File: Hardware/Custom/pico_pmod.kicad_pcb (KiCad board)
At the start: 2 copper layers, 50 x 37 mm, 35 parts, among them J1 Conn_02x06_Odd_Even, J2 Conn_02x06_Odd_Even, J3 Conn_02x06_Odd_Even, J4 USB_C_Receptacle_USB2.0, J5 Conn_01x04, SW1 SW_Push, SW2 SW_Push, U1 RP2040, U2 W25Q128JVS, U3 NCP1117-3.3_SOT223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

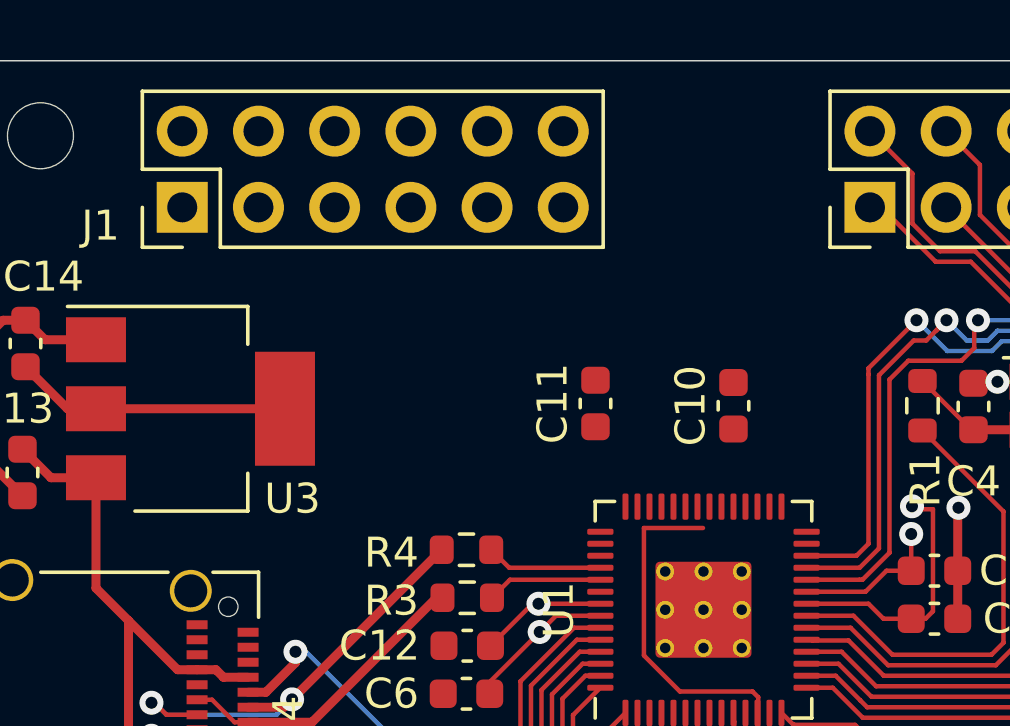
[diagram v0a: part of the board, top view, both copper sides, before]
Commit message: Add connections to PMOD1A connector
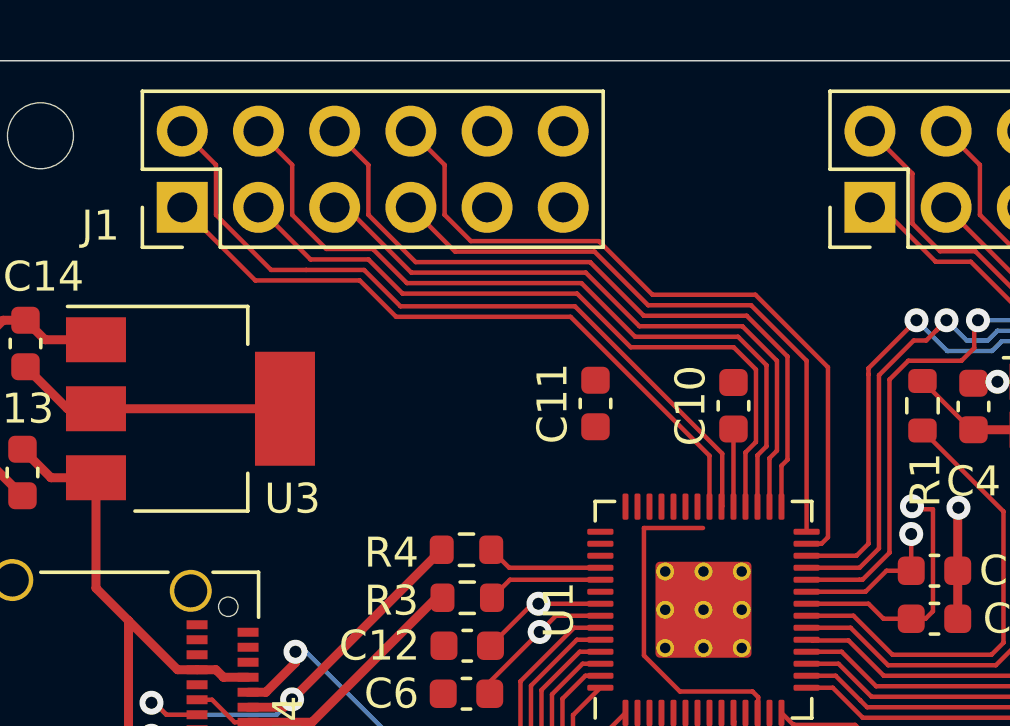
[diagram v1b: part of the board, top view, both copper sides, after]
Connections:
- J1 pad 1: Net-(J1-Pad1) -> GPIO_23
- J1 pad 2: Net-(J1-Pad2) -> GPIO_22
- J1 pad 3: Net-(J1-Pad3) -> GPIO_21
- J1 pad 4: Net-(J1-Pad4) -> GPIO_20
- J1 pad 5: Net-(J1-Pad5) -> GPIO_19
- J1 pad 6: Net-(J1-Pad6) -> GPIO_18
- J1 pad 7: Net-(J1-Pad7) -> GPIO_17
- J1 pad 8: Net-(J1-Pad8) -> GPIO_16
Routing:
- net GPIO_20: track 0.00 -> 26.0 mm
- net GPIO_22: track 0.00 -> 25.2 mm
- net GPIO_16: track 0.00 -> 24.6 mm
- net GPIO_18: track 0.00 -> 24.3 mm
- net GPIO_21: track 0.00 -> 23.5 mm
- net GPIO_23: track 0.00 -> 22.7 mm
- net GPIO_19: track 0.00 -> 21.8 mm
- net GPIO_17: track 0.00 -> 21.0 mm
- net +3V3: track 47.2 -> 49.8 mm

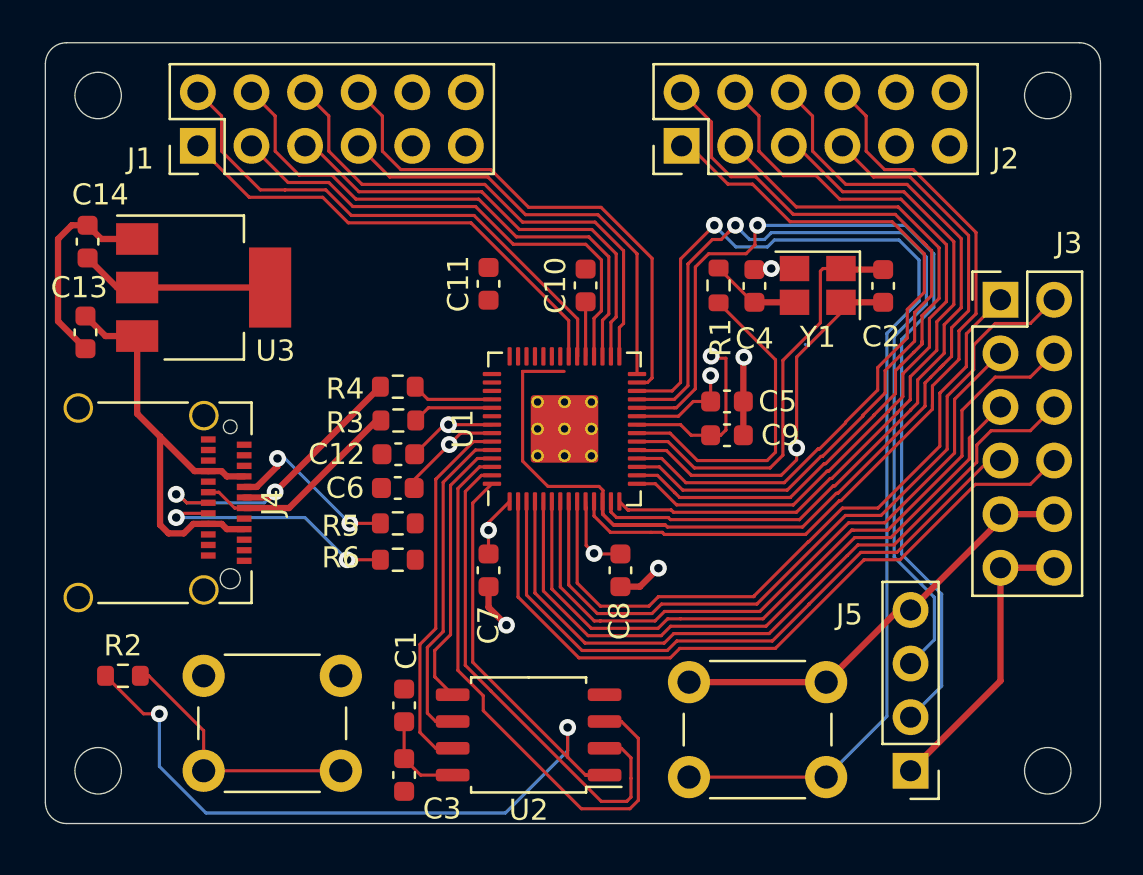
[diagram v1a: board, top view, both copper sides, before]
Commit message: update with ground plane and LED's
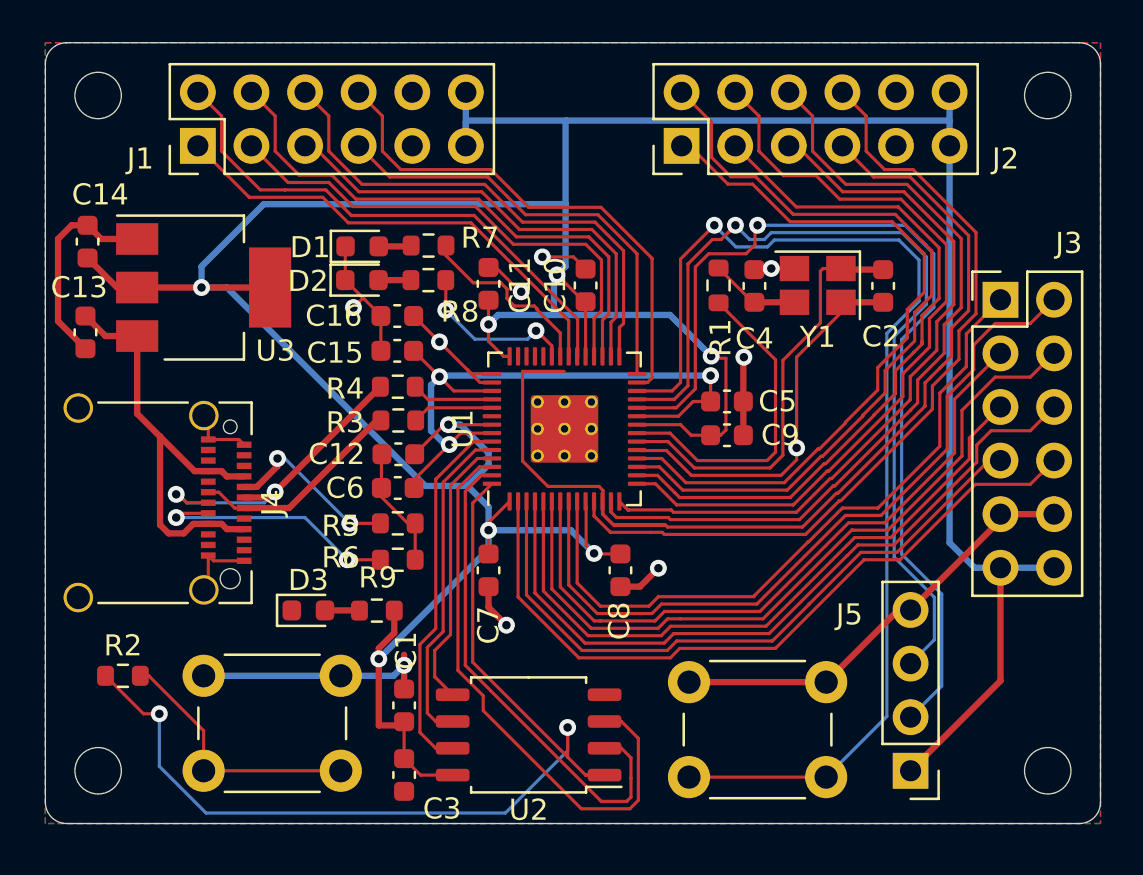
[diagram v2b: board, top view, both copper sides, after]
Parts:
- added C15: 1u, Capacitor_SMD:C_0603_1608Metric, F.Cu at (139.7, 71.6)
- added C16: 1u, Capacitor_SMD:C_0603_1608Metric, F.Cu at (139.7, 70.0)
- added D1: LED, LED_SMD:LED_0603_1608Metric, F.Cu at (138.0, 66.7)
- added D2: LED, LED_SMD:LED_0603_1608Metric, F.Cu at (138.0, 68.2)
- added D3: LED, LED_SMD:LED_0603_1608Metric, F.Cu at (135.5, 83.9)
- added R7: R, Resistor_SMD:R_0603_1608Metric, F.Cu at (141.2, 66.6)
- added R8: R, Resistor_SMD:R_0603_1608Metric, F.Cu at (141.2, 68.2)
- added R9: R, Resistor_SMD:R_0603_1608Metric, F.Cu at (138.7, 83.9)
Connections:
- U1 pad 37: Net-(U1-Pad37) -> GPIO_25
- U1 pad 43: Net-(U1-Pad43) -> +3V3
- U1 pad 44: Net-(U1-Pad44) -> +3V3
- U1 pad 45: Net-(U1-Pad45) -> +1V1
- U1 pad 48: Net-(U1-Pad48) -> +3V3
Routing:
- net +3V3: track 49.8 -> 196.7 mm, vias 4 -> 9
- net GND: track 59.5 -> 93.4 mm, vias 5 -> 9
- net +1V1: track 10.0 -> 31.3 mm, vias 2 -> 3
- net GPIO_24: track 0.00 -> 8.82 mm
- net GPIO_25: track 0.00 -> 7.98 mm, vias 0 -> 2
- net Net-(D3-Pad2): track 0.00 -> 1.64 mm
- net Net-(D1-Pad2): track 0.00 -> 1.55 mm
- net Net-(D2-Pad2): track 0.00 -> 1.54 mm
- added copper zone on B.Cu, net GND
- added copper zone on F.Cu, net GND

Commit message: Add the logo and text onto back of the PCB
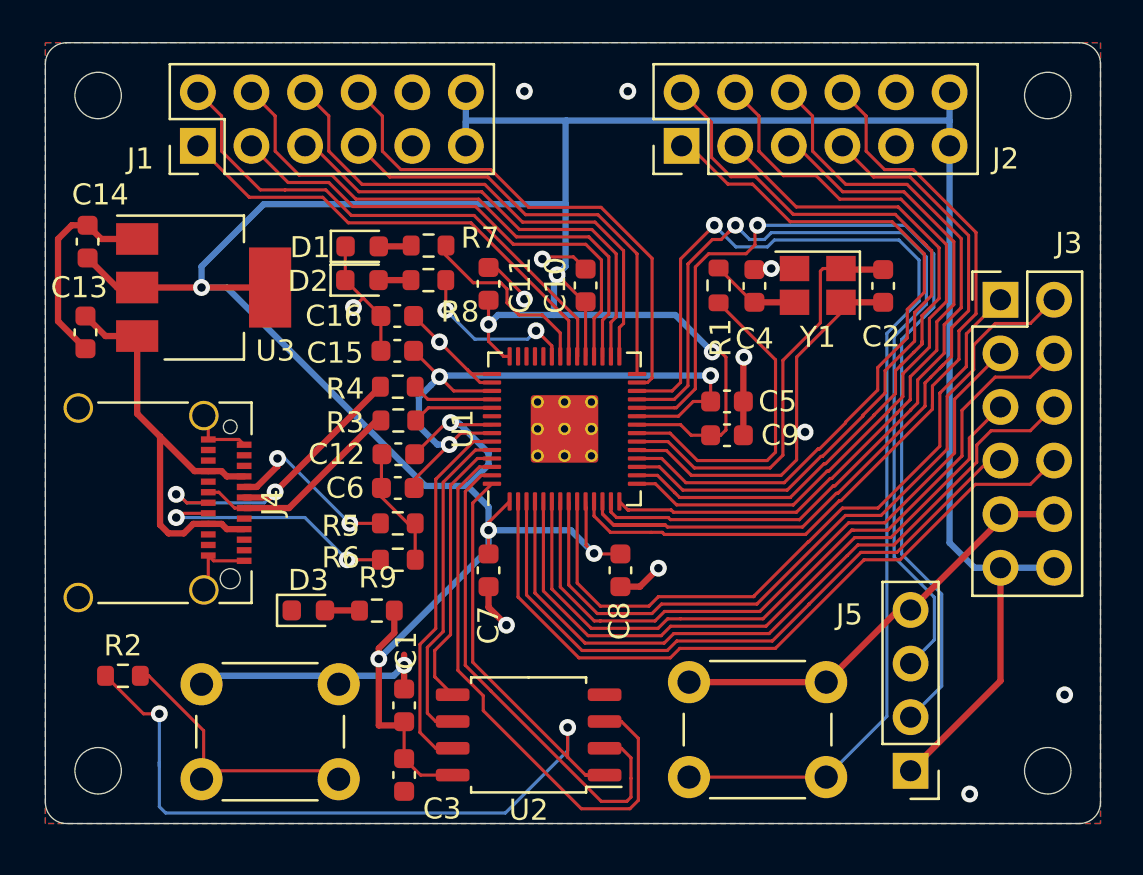
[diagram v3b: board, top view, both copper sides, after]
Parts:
- added G***: LOGO, jjh:Untitled, B.Cu at (155.0, 76.2)
- moved SW1 0.41 mm to (130.4, 87.4)
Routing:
- net GPIO_9: track 50.3 -> 38.6 mm
- net QSPI_SS: track 47.9 -> 49.2 mm
- net +1V1: track 31.3 -> 32.2 mm
- net GND: track 93.4 -> 94.3 mm, vias 9 -> 13
- net +3V3: track 196.7 -> 197.3 mm
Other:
- board text added: "RP2040 PMod Board @jamesjhorton jjhorton.co.uk"

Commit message: Add lables to the Debug Port
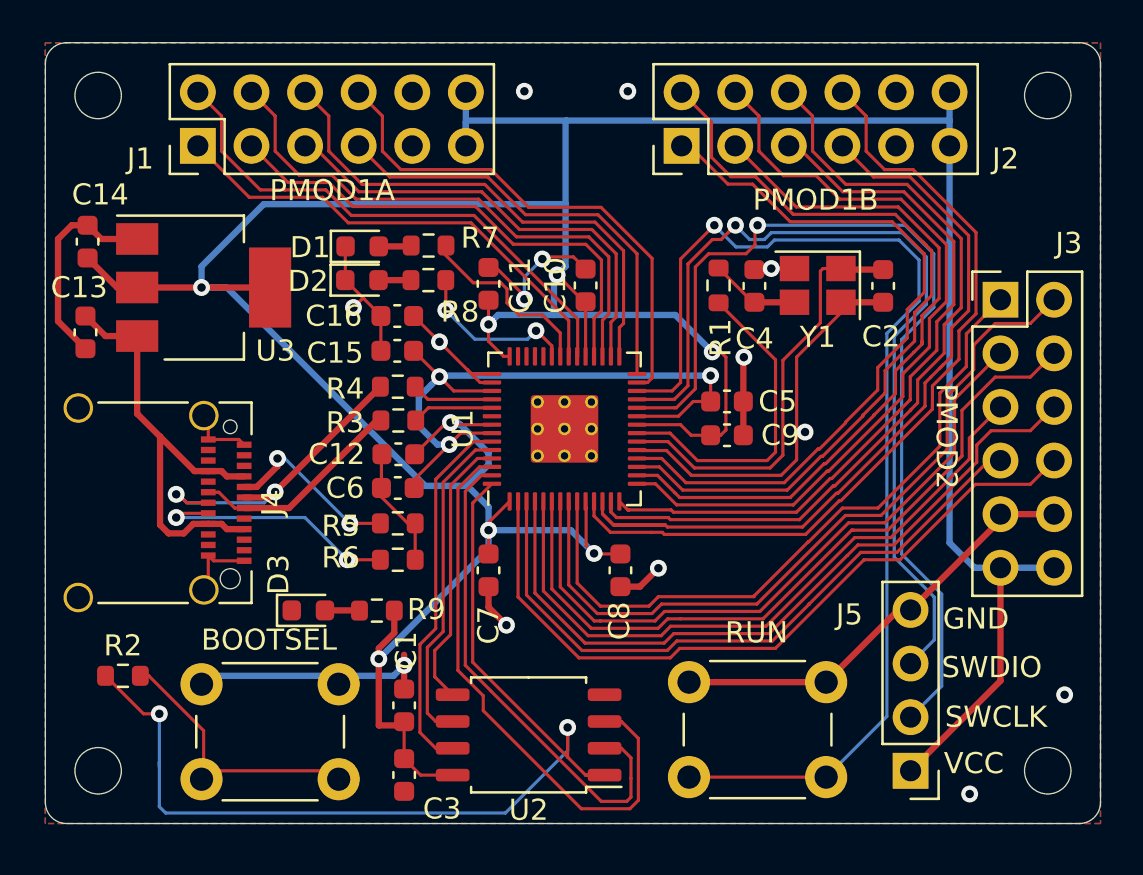
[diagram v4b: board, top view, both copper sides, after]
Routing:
- net GND: track 94.3 -> 96.5 mm
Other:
- board text added: "BOOTSEL"
- board text added: "GND"
- board text added: "PMOD1A"
- board text added: "PMOD1B"
- board text added: "PMOD2"
- board text added: "RUN"
- board text added: "SWCLK"
- board text added: "SWDIO"
- board text added: "VCC"
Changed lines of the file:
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@@
   (general
     (thickness 1.6)
-    (drawings 15)
-    (tracks 779)
+    (drawings 24)
+    (tracks 781)
     (zones 0)
     (modules 44)
@@
   (page A4)
   (layers
-    (0 F.Cu signal)
-    (31 B.Cu signal)
+    (0 F.Cu signal hide)
+    (31 B.Cu signal hide)
     (32 B.Adhes user)
     (33 F.Adhes user)
     (34 B.Paste user)
     (35 F.Paste user)
-    (36 B.SilkS user)
+    (36 B.SilkS user hide)
     (37 F.SilkS user)
     (38 B.Mask user)
@@
     (tags resistor)
     (attr smd)
-    (fp_text reference R9 (at -0.04 1.56) (layer F.SilkS)
+    (fp_text reference R9 (at -2.34 0.06) (layer F.SilkS)
       (effects (font (size 1 1) (thickness 0.15)))
     )
@@
     (tags LED)
     (attr smd)
-    (fp_text reference D3 (at 0 -1.43) (layer F.SilkS)
+    (fp_text reference D3 (at -1.4125 -1.7 90) (layer F.SilkS)
       (effects (font (size 1 1) (thickness 0.15)))
     )
@@
       (rotate (xyz 0 0 0))
     )
+  )
+  (gr_text GND (at 167.1 84.3) (layer F.SilkS)
+    (effects (font (size 1 1) (thickness 0.25)))
+  )
+  (gr_text SWDIO (at 167.85 86.6) (layer F.SilkS)
+    (effects (font (size 1 1) (thickness 0.25)))
+  )
+  (gr_text "SWCLK\n" (at 168.05 88.95) (layer F.SilkS)
+    (effects (font (size 1 1) (thickness 0.25)))
+  )
+  (gr_text VCC (at 167 91.15) (layer F.SilkS)
+    (effects (font (size 1 1) (thickness 0.25)))
+  )
+  (gr_text PMOD1A (at 136.6 64) (layer F.SilkS)
+    (effects (font (size 1 1) (thickness 0.25)))
+  )
+  (gr_text PMOD1B (at 159.5 64.45) (layer F.SilkS)
+    (effects (font (size 1 1) (thickness 0.25)))
+  )
+  (gr_text PMOD2 (at 165.7 75.65 270) (layer F.SilkS)
+    (effects (font (size 1 1) (thickness 0.25)))
+  )
+  (gr_text BOOTSEL (at 133.6 85.3) (layer F.SilkS)
+    (effects (font (size 1 1) (thickness 0.25)))
+  )
+  (gr_text RUN (at 156.7 84.95) (layer F.SilkS)
+    (effects (font (size 1 1) (thickness 0.25)))
   )
   (gr_text "RP2040 \nPMod Board\n@jamesjhorton\njjhorton.co.uk" (at 139.95 75.75) (layer B.SilkS)
@@
   (segment (start 144.35 67.65) (end 145.7 69) (width 0.15) (layer F.Cu) (net 1))
   (segment (start 144 67.65) (end 144.35 67.65) (width 0.15) (layer F.Cu) (net 1))
+  (segment (start 145.7 68.1) (end 146.55 67.25) (width 0.15) (layer B.Cu) (net 1))
+  (segment (start 145.7 69.15) (end 145.7 68.1) (width 0.15) (layer B.Cu) (net 1))
   (segment (start 140 90.925) (end 140.78 91.705) (width 0.15) (layer F.Cu) (net 2))
   (segment (start 140.78 91.705) (end 142.3 91.705) (width 0.15) (layer F.Cu) (net 2))

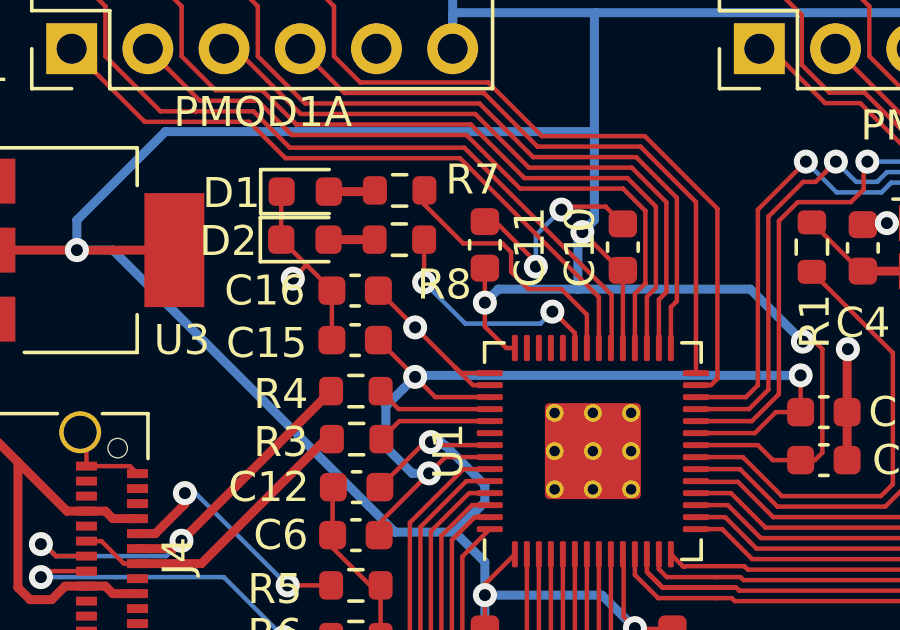
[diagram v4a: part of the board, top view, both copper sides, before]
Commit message: fix DRC errors with 3v3 power
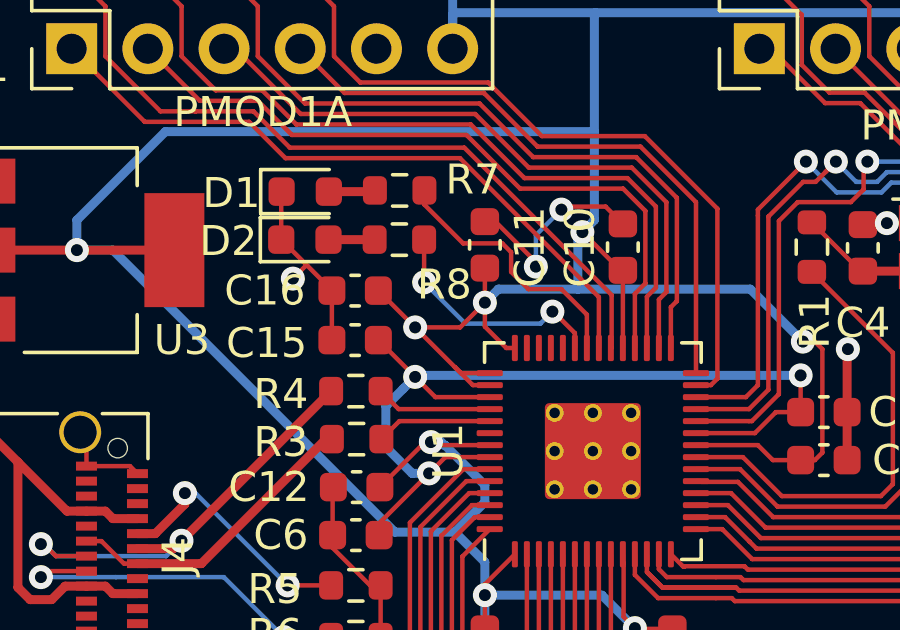
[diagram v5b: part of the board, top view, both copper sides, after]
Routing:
- net +3V3: track 197.3 -> 200.0 mm
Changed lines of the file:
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@@
     (thickness 1.6)
     (drawings 24)
-    (tracks 781)
+    (tracks 783)
     (zones 0)
     (modules 44)
@@
   (page A4)
   (layers
-    (0 F.Cu signal hide)
-    (31 B.Cu signal hide)
+    (0 F.Cu signal)
+    (31 B.Cu signal)
     (32 B.Adhes user)
     (33 F.Adhes user)
@@
     (mod_text_size 1 1)
     (mod_text_width 0.15)
-    (pad_size 1.524 1.524)
-    (pad_drill 0.762)
+    (pad_size 1.4 1.4)
+    (pad_drill 1.1)
     (pad_to_mask_clearance 0)
     (aux_axis_origin 0 0)
@@
   (segment (start 155 75.6) (end 155.25001 75.34999) (width 0.15) (layer F.Cu) (net 2))
   (segment (start 154.525 75.6) (end 155 75.6) (width 0.15) (layer F.Cu) (net 2))
+  (segment (start 143.175 71.175) (end 144 70.35) (width 0.15) (layer F.Cu) (net 2))
+  (segment (start 141.675 71.175) (end 143.175 71.175) (width 0.15) (layer F.Cu) (net 2))
   (segment (start 160.75 67.75) (end 160.7 67.7) (width 0.3) (layer F.Cu) (net 3))
   (segment (start 162.7 67.75) (end 160.75 67.75) (width 0.3) (layer F.Cu) (net 3))
